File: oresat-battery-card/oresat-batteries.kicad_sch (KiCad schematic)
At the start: 11 parts, among them J1 J-SAMTEC-TFM-120-X1-XXX-D-RA, SW1 D2F-L3-D (LEFT), SW2 D2F-L3-D (RIGHT), SW3 D2F-L3-D (LEFT), SW4 D2F-L3-D (RIGHT)

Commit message: Jumped back on the TPS bandwagon - LCSC to the rescue! - and lots of cleanup.
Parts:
- added D15: B330A-13-F, Diode_SMD:D_SMA, symbol Device:D_Schottky_Filled
- SW1, SW3: value D2F-L3-D (LEFT) -> D2F-L3-D3 (LEFT); footprint oresat-misc:D2F-L3-D-HORIZONTAL-L -> oresat-misc:D2F-L3-D3-HORIZONTAL-L; DPN SW1443-ND -> Z8531-ND; MFR Oron Electronics -> Aratas (Formerly Omron Components); MPN SW1443-ND -> D2F-L3-D3
- SW2, SW4: value D2F-L3-D (RIGHT) -> D2F-L3-D3 (RIGHT); footprint oresat-misc:D2F-L3-D-HORIZONTAL-R -> oresat-misc:D2F-L3-D3-HORIZONTAL-R; DPN SW1443-ND -> Z8531-ND; MFR Oron Electronics -> Aratas (Formerly Omron Components); MPN SW1443-ND -> D2F-L3-D3
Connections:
- net GND: now also D15.2 (A)
- net INH-POS-BATT-DISC: now also SW3.NO; no longer SW3.NC
- net VBUS: now also D15.1 (K)
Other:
- note added: "+X+Y"
- note added: "2x OMRON D2F-5L3 SPDT Switch"
- note added: "NEGATIVE BATTERY DISCONNECT: Normally closed switch enables MOSFET; press to disconnect and turn off MOSFET."
- note added: "POSITIVE BATTERY DISCONNECT: Normally open switch enables eFUSE; press to disable eFUSE."
- note removed: "2x OMRON D2F-5L3 SPDT Switch (COM + NC connected)"
- note removed: "Normally Closed inhibit switches (disconnects VBAT from VBUS when pressed)"
- moved on the sheet: SW3

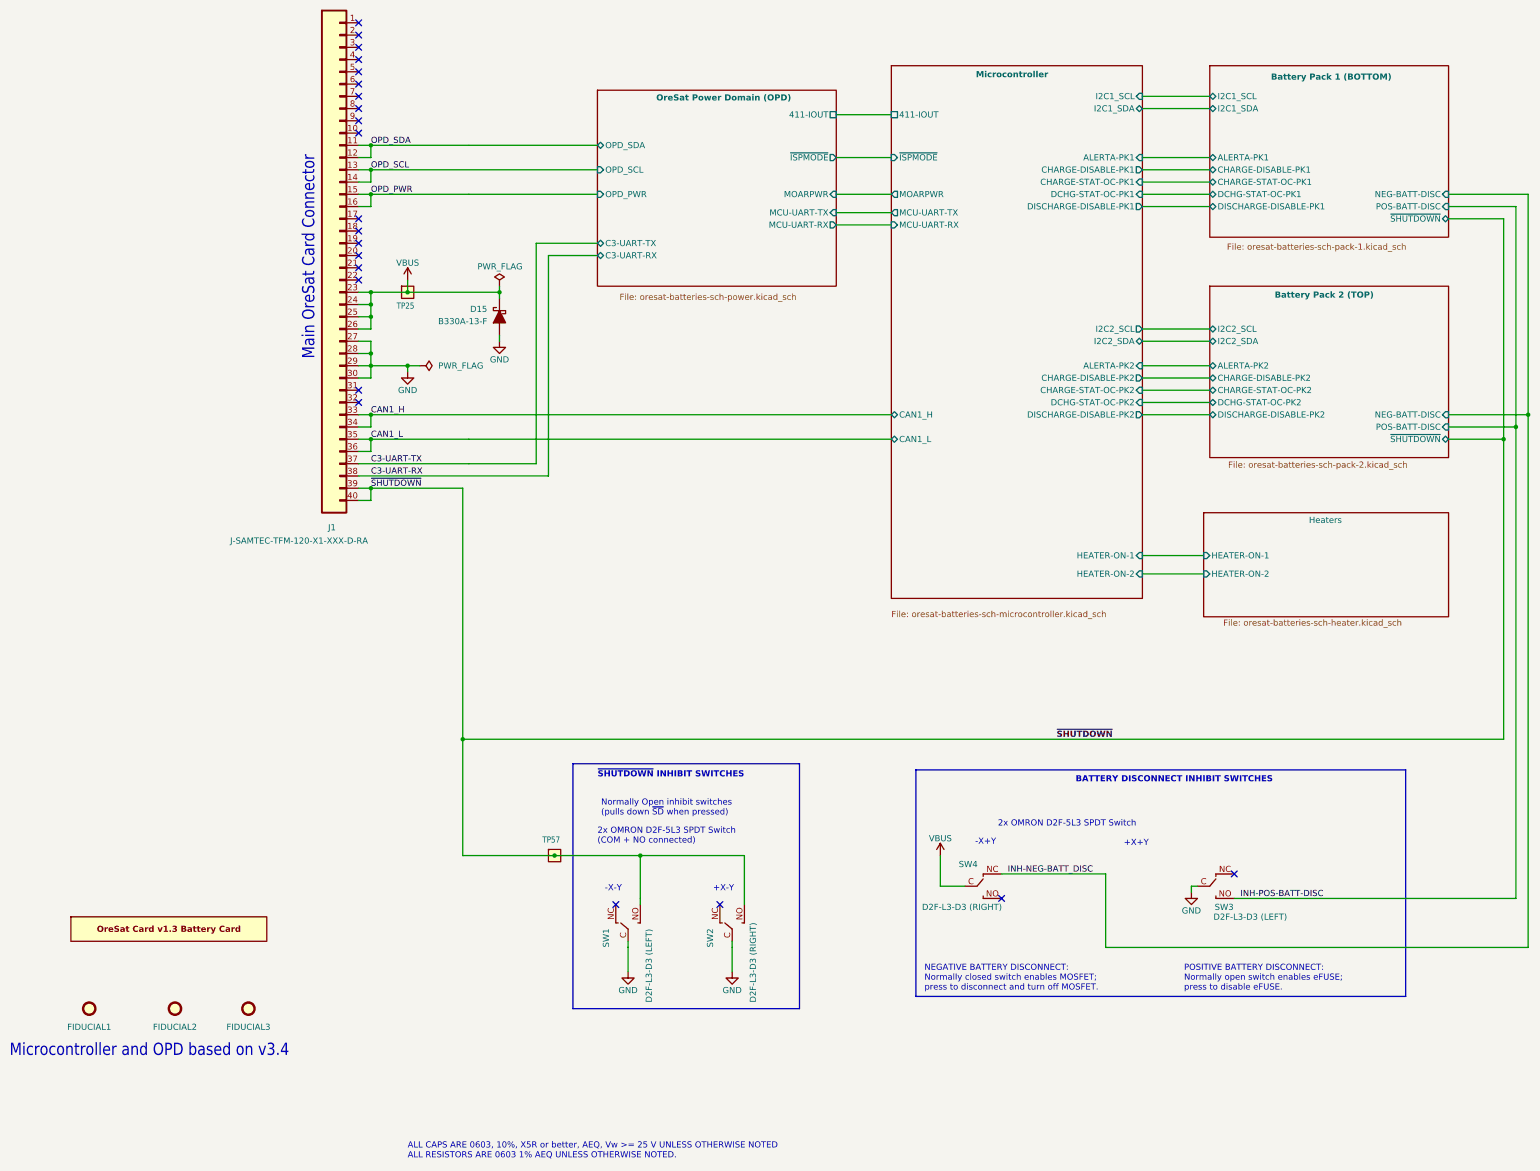
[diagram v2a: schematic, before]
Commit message: Updated Makefile and Readme; fixed TCAN IC, cleanup, fix battery connections that were killed somehow
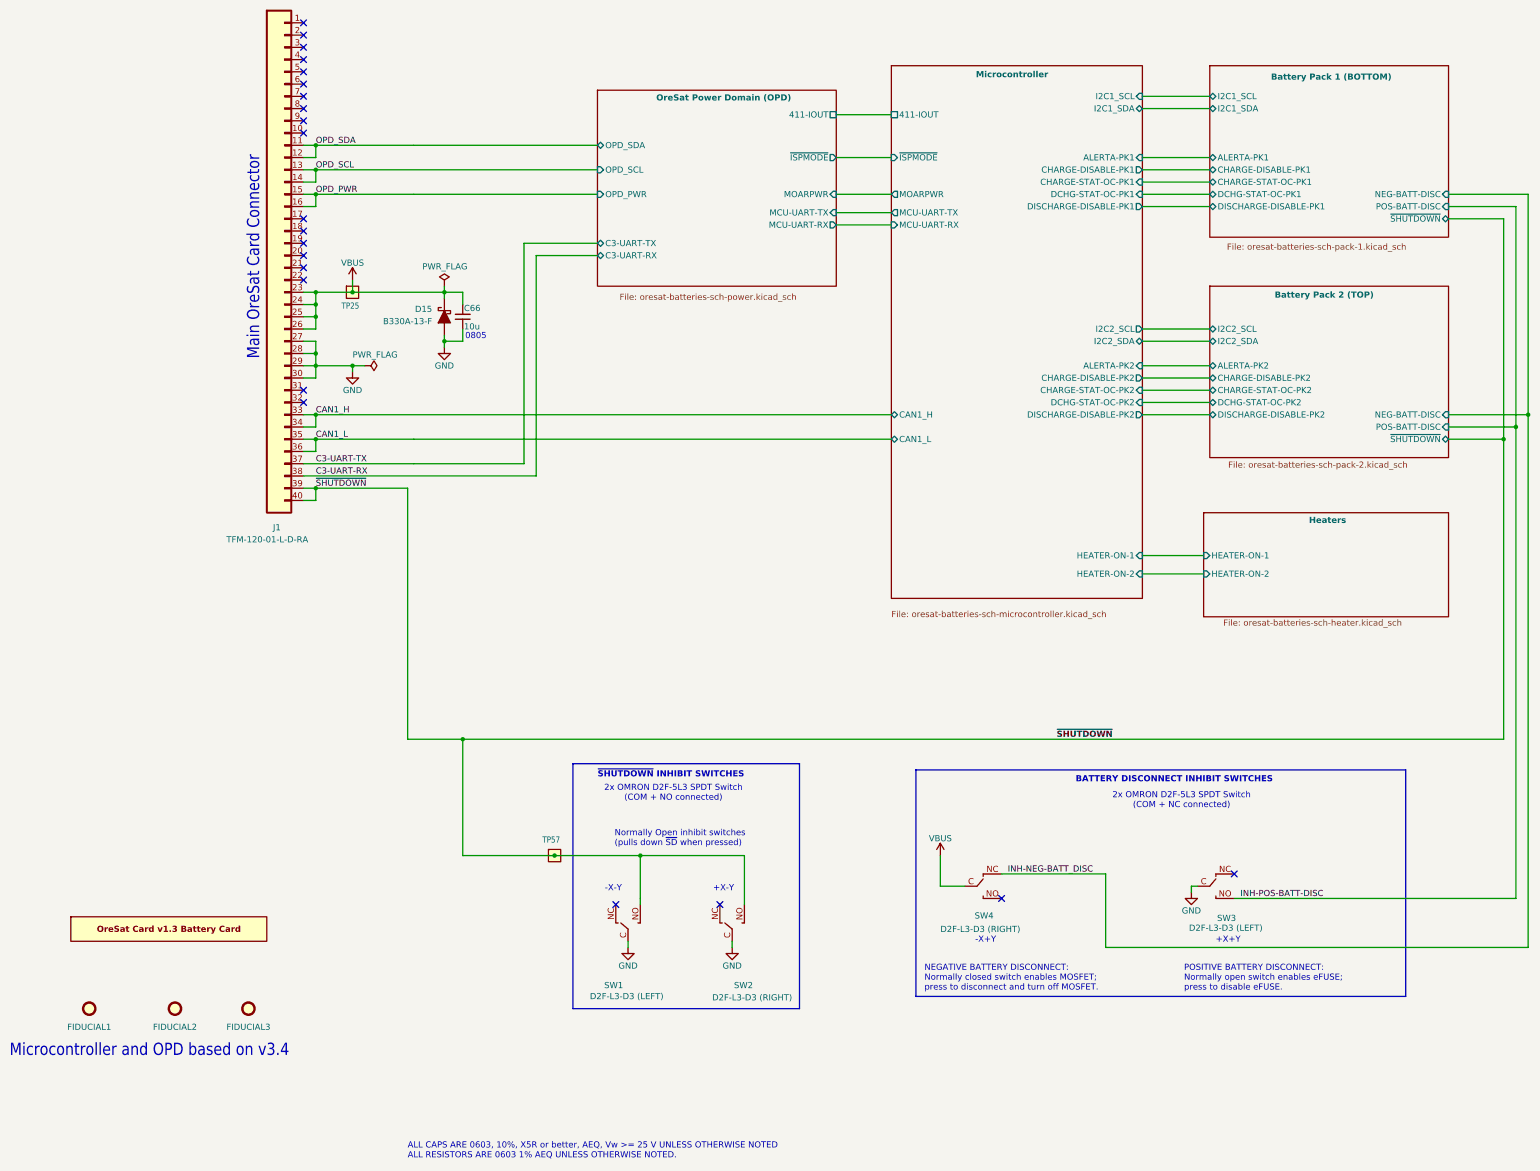
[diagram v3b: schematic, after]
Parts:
- added C66: 10u, oresat-passives:0805-C-NOSILK, symbol Device:C_Small
- J1: value J-SAMTEC-TFM-120-X1-XXX-D-RA -> TFM-120-01-L-D-RA
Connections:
- net GND: now also C66.2
- net VBUS: now also C66.1
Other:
- note added: "0805"
- note added: "2x OMRON D2F-5L3 SPDT Switch (COM + NC connected)"
- note removed: "2x OMRON D2F-5L3 SPDT Switch"
- moved on the sheet: D15, J1, TP25

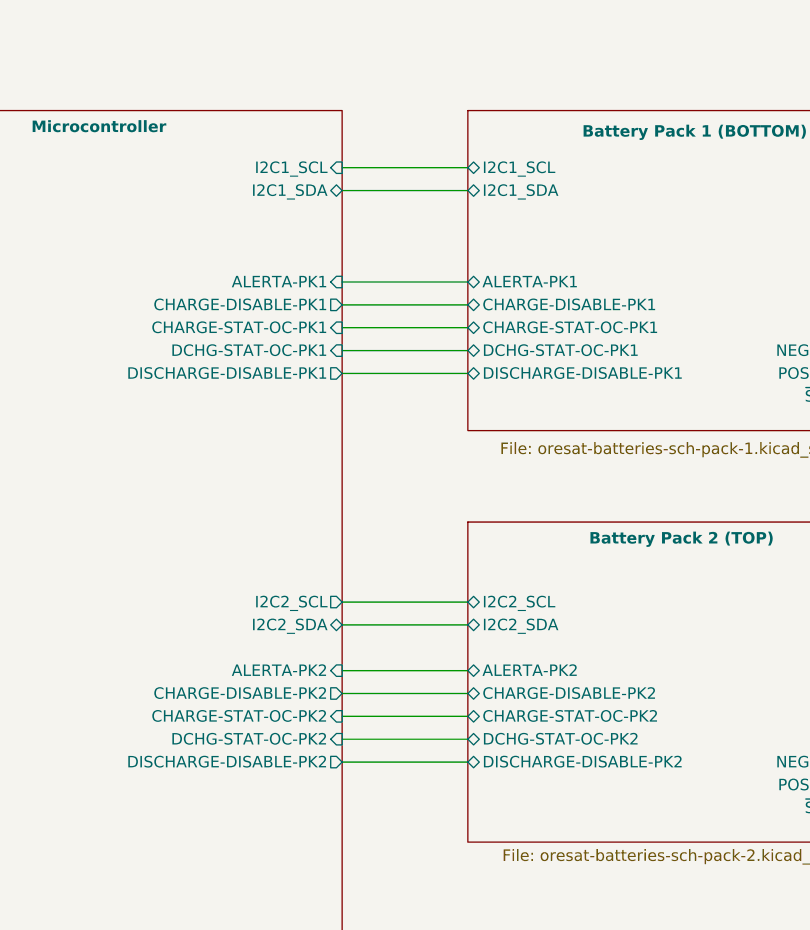
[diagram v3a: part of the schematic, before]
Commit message: Added imon capabilities, cleaned up some lingering DRCs that kept popping back up.
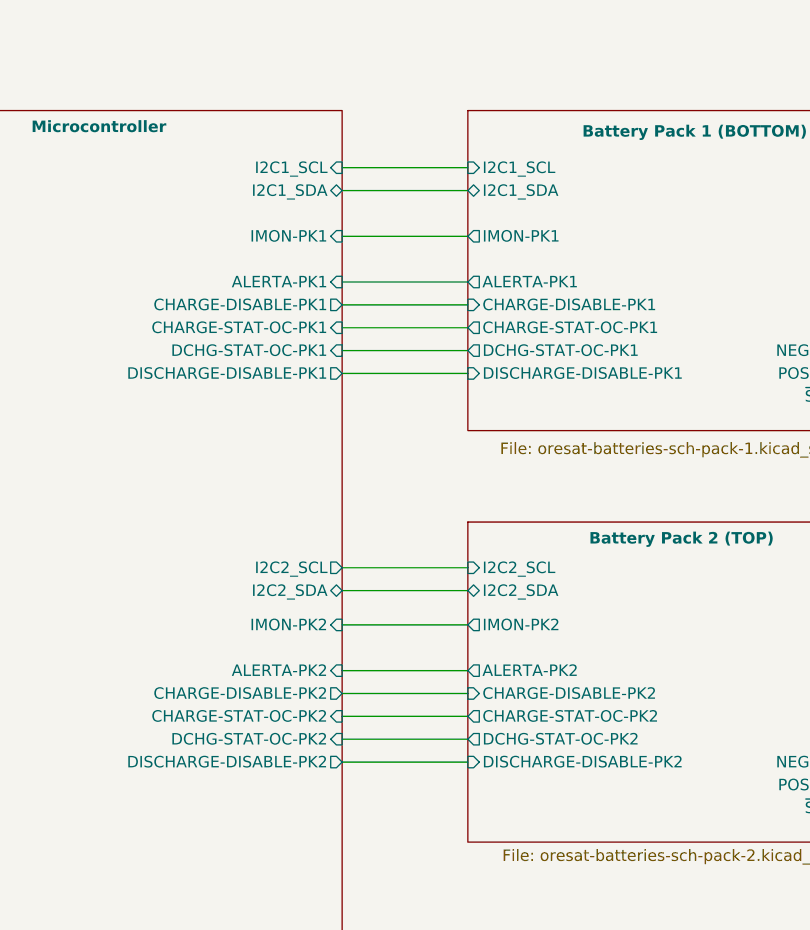
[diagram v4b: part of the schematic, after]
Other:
- sheet Battery Pack 1 (BOTTOM) ports: added IMON-PK1; removed none
- sheet Battery Pack 2 (TOP) ports: added IMON-PK2; removed none
- sheet Microcontroller ports: added IMON-PK1, IMON-PK2; removed none
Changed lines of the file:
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@@
 	(wire
 		(pts
+			(xy 265.43 96.52) (xy 279.4 96.52)
+		)
+		(stroke
+			(width 0)
+			(type default)
+		)
+	)
+	(wire
+		(pts
 			(xy 91.44 119.38) (xy 93.98 119.38)
 		)
@@
 	(wire
 		(pts
+			(xy 265.43 53.34) (xy 279.4 53.34)
+		)
+		(stroke
+			(width 0)
+			(type default)
+		)
+	)
+	(wire
+		(pts
 			(xy 93.98 88.9) (xy 91.44 88.9)
 		)
@@
 	(wire
 		(pts
-			(xy 265.43 93.98) (xy 279.4 93.98)
+			(xy 265.43 90.17) (xy 279.4 90.17)
 		)
 		(stroke
@@
 	(wire
 		(pts
-			(xy 265.43 96.52) (xy 279.4 96.52)
+			(xy 265.43 92.71) (xy 279.4 92.71)
 		)
 		(stroke
@@
 		)
 		(pin "I2C2_SCL" output
-			(at 265.43 93.98 0)
+			(at 265.43 90.17 0)
 			(effects
 				(font
@@
 		)
 		(pin "I2C2_SDA" bidirectional
-			(at 265.43 96.52 0)
+			(at 265.43 92.71 0)
 			(effects
 				(font
@@
 			)
 		)
+		(pin "IMON-PK1" input
+			(at 265.43 53.34 0)
+			(effects
+				(font
+					(size 1.27 1.27)
+				)
+				(justify right)
+			)
+		)
+		(pin "IMON-PK2" input
+			(at 265.43 96.52 0)
+			(effects
+				(font
+					(size 1.27 1.27)
+				)
+				(justify right)
+			)
+		)
 		(instances
 			(project "oresat-batteries"
@@
 			)
 		)
-		(pin "ALERTA-PK2" bidirectional
+		(pin "ALERTA-PK2" output
 			(at 279.4 101.6 180)
 			(effects
@@
 			)
 		)
-		(pin "CHARGE-DISABLE-PK2" bidirectional
+		(pin "CHARGE-DISABLE-PK2" input
 			(at 279.4 104.14 180)
 			(effects
@@
 			)
 		)
-		(pin "CHARGE-STAT-OC-PK2" bidirectional
+		(pin "CHARGE-STAT-OC-PK2" output
 			(at 279.4 106.68 180)
 			(effects
@@
 			)
 		)
-		(pin "DCHG-STAT-OC-PK2" bidirectional
+		(pin "DCHG-STAT-OC-PK2" output
 			(at 279.4 109.22 180)
 			(effects
@@
 			)
 		)
-		(pin "DISCHARGE-DISABLE-PK2" bidirectional
+		(pin "DISCHARGE-DISABLE-PK2" input
 			(at 279.4 111.76 180)
 			(effects
@@
 			)
 		)
-		(pin "I2C2_SCL" bidirectional
-			(at 279.4 93.98 180)
+		(pin "I2C2_SCL" input
+			(at 279.4 90.17 180)
 			(effects
 				(font
@@
 		)
 		(pin "I2C2_SDA" bidirectional
-			(at 279.4 96.52 180)
+			(at 279.4 92.71 180)
 			(effects
 				(font
@@
 			)
 		)
+		(pin "IMON-PK2" output
+			(at 279.4 96.52 180)
+			(effects
+				(font
+					(size 1.27 1.27)
+				)
+				(justify left)
+			)
+		)
 		(instances
 			(project "oresat-batteries"
@@
 			)
 		)
-		(pin "I2C1_SCL" bidirectional
+		(pin "I2C1_SCL" input
 			(at 279.4 45.72 180)
 			(effects
@@
 			)
 		)
-		(pin "ALERTA-PK1" bidirectional
+		(pin "ALERTA-PK1" output
 			(at 279.4 58.42 180)
 			(effects
@@
 			)
 		)
-		(pin "CHARGE-DISABLE-PK1" bidirectional
+		(pin "CHARGE-DISABLE-PK1" input
 			(at 279.4 60.96 180)
 			(effects
@@
 			)
 		)
-		(pin "CHARGE-STAT-OC-PK1" bidirectional
+		(pin "CHARGE-STAT-OC-PK1" output
 			(at 279.4 63.5 180)
 			(effects
@@
 			)
 		)
-		(pin "DCHG-STAT-OC-PK1" bidirectional
+		(pin "DCHG-STAT-OC-PK1" output
 			(at 279.4 66.04 180)
 			(effects
@@
 			)
 		)
-		(pin "DISCHARGE-DISABLE-PK1" bidirectional
+		(pin "DISCHARGE-DISABLE-PK1" input
 			(at 279.4 68.58 180)
 			(effects
@@
 			)
 		)
+		(pin "IMON-PK1" output
+			(at 279.4 53.34 180)
+			(effects
+				(font
+					(size 1.27 1.27)
+				)
+				(justify left)
+			)
+		)
